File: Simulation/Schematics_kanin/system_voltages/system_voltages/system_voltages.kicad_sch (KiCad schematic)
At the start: 1 part

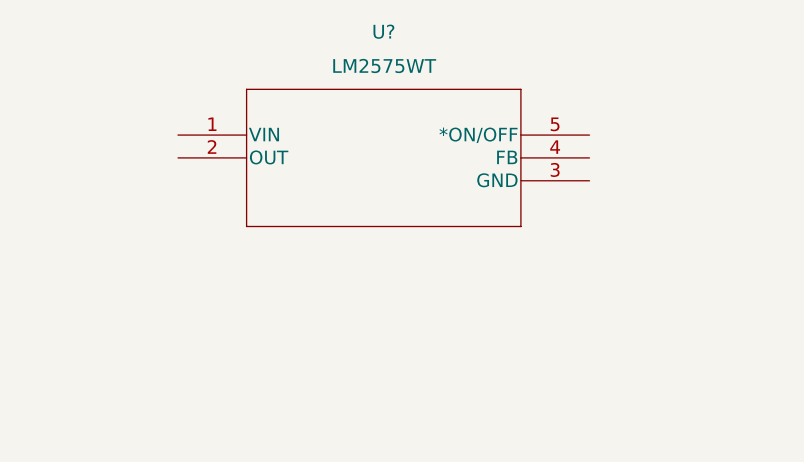
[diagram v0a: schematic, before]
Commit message: Made some changes for system voltages
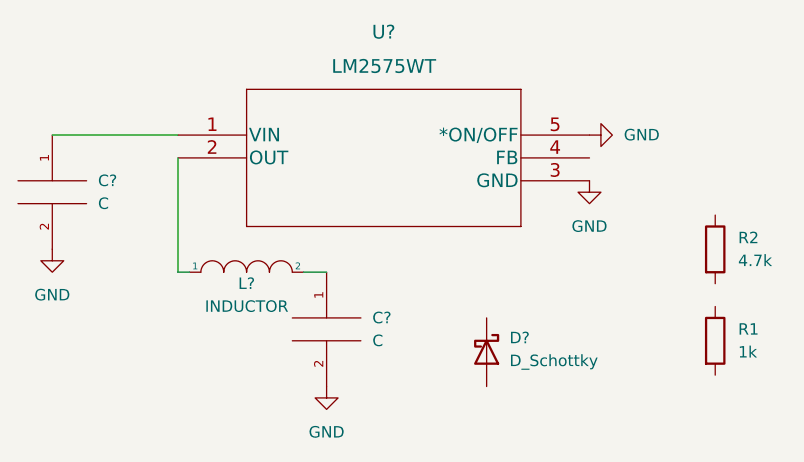
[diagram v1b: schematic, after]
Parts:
- added C? (x2): C, symbol pspice:C
- added D?: D_Schottky, symbol Device:D_Schottky
- added L?: INDUCTOR, symbol pspice:INDUCTOR
- added R1: 1k, symbol Device:R
- added R2: 4.7k, symbol Device:R
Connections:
- net at U?.1 (VIN): now also C?.1
- net at U?.2 (OUT): now also L?.1
- net GND: now reaches U?.3 (GND)
- net GND: now also U?.5 (*ON/OFF), C?.2, C?.2
- new net: C?.1, L?.2
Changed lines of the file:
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@@
 (kicad_sch (version 20211123) (generator eeschema)
   (paper "A4")
+  (wire (pts (xy 132.08 118.11) (xy 134.62 118.11))
+    (stroke (width 0) (type default) (color 0 0 0 0))
+  )
+  (wire (pts (xy 104.14 102.87) (xy 118.11 102.87))
+    (stroke (width 0) (type default) (color 0 0 0 0))
+  )
+  (wire (pts (xy 118.11 118.11) (xy 119.38 118.11))
+    (stroke (width 0) (type default) (color 0 0 0 0))
+  )
+  (wire (pts (xy 118.11 105.41) (xy 118.11 118.11))
+    (stroke (width 0) (type default) (color 0 0 0 0))
+  )
+  (symbol (lib_id "Device:D_Schottky") (at 152.4 127 270) (unit 1)
+    (in_bom yes) (on_board yes) (fields_autoplaced)
+    (property "Reference" "D?" (id 0) (at 154.94 125.4124 90)
+      (effects (font (size 1.27 1.27)) (justify left))
+    )
+    (property "Value" "D_Schottky" (id 1) (at 154.94 127.9524 90)
+      (effects (font (size 1.27 1.27)) (justify left))
+    )
+    (property "Footprint" "" (id 2) (at 152.4 127 0)
+      (effects (font (size 1.27 1.27)) hide)
+    )
+    (property "Datasheet" "~" (id 3) (at 152.4 127 0)
+      (effects (font (size 1.27 1.27)) hide)
+    )
+    (pin "1")
+    (pin "2")
+  )
   (symbol (lib_id "LM2575WT:LM2575WT") (at 118.11 102.87 0) (unit 1)
     (in_bom yes) (on_board yes) (fields_autoplaced)
@@
     (pin "5")
   )
+  (symbol (lib_id "power:GND") (at 163.83 107.95 0) (unit 1)
+    (in_bom yes) (on_board yes) (fields_autoplaced)
+    (property "Reference" "#PWR?" (id 0) (at 163.83 114.3 0)
+      (effects (font (size 1.27 1.27)) hide)
+    )
+    (property "Value" "GND" (id 1) (at 163.83 113.03 0))
+    (property "Footprint" "" (id 2) (at 163.83 107.95 0)
+      (effects (font (size 1.27 1.27)) hide)
+    )
+    (property "Datasheet" "" (id 3) (at 163.83 107.95 0)
+      (effects (font (size 1.27 1.27)) hide)
+    )
+    (pin "1")
+  )
+  (symbol (lib_id "Device:R") (at 177.8 115.57 0) (unit 1)
+    (in_bom yes) (on_board yes) (fields_autoplaced)
+    (property "Reference" "R2" (id 0) (at 180.34 114.2999 0)
+      (effects (font (size 1.27 1.27)) (justify left))
+    )
+    (property "Value" "4.7k" (id 1) (at 180.34 116.8399 0)
+      (effects (font (size 1.27 1.27)) (justify left))
+    )
+    (property "Footprint" "" (id 2) (at 176.022 115.57 90)
+      (effects (font (size 1.27 1.27)) hide)
+    )
+    (property "Datasheet" "~" (id 3) (at 177.8 115.57 0)
+      (effects (font (size 1.27 1.27)) hide)
+    )
+    (pin "1")
+    (pin "2")
+  )
+  (symbol (lib_id "power:GND") (at 163.83 102.87 90) (unit 1)
+    (in_bom yes) (on_board yes) (fields_autoplaced)
+    (property "Reference" "#PWR?" (id 0) (at 170.18 102.87 0)
+      (effects (font (size 1.27 1.27)) hide)
+    )
+    (property "Value" "GND" (id 1) (at 167.64 102.8699 90)
+      (effects (font (size 1.27 1.27)) (justify right))
+    )
+    (property "Footprint" "" (id 2) (at 163.83 102.87 0)
+      (effects (font (size 1.27 1.27)) hide)
+    )
+    (property "Datasheet" "" (id 3) (at 163.83 102.87 0)
+      (effects (font (size 1.27 1.27)) hide)
+    )
+    (pin "1")
+  )
+  (symbol (lib_id "pspice:C") (at 134.62 124.46 0) (unit 1)
+    (in_bom yes) (on_board yes) (fields_autoplaced)
+    (property "Reference" "C?" (id 0) (at 139.7 123.1899 0)
+      (effects (font (size 1.27 1.27)) (justify left))
+    )
+    (property "Value" "C" (id 1) (at 139.7 125.7299 0)
+      (effects (font (size 1.27 1.27)) (justify left))
+    )
+    (property "Footprint" "" (id 2) (at 134.62 124.46 0)
+      (effects (font (size 1.27 1.27)) hide)
+    )
+    (property "Datasheet" "~" (id 3) (at 134.62 124.46 0)
+      (effects (font (size 1.27 1.27)) hide)
+    )
+    (pin "1")
+    (pin "2")
+  )
+  (symbol (lib_id "power:GND") (at 134.62 130.81 0) (unit 1)
+    (in_bom yes) (on_board yes) (fields_autoplaced)
+    (property "Reference" "#PWR?" (id 0) (at 134.62 137.16 0)
+      (effects (font (size 1.27 1.27)) hide)
+    )
+    (property "Value" "GND" (id 1) (at 134.62 135.89 0))
+    (property "Footprint" "" (id 2) (at 134.62 130.81 0)
+      (effects (font (size 1.27 1.27)) hide)
+    )
+    (property "Datasheet" "" (id 3) (at 134.62 130.81 0)
+      (effects (font (size 1.27 1.27)) hide)
+    )
+    (pin "1")
+  )
+  (symbol (lib_id "power:GND") (at 104.14 115.57 0) (unit 1)
+    (in_bom yes) (on_board yes) (fields_autoplaced)
+    (property "Reference" "#PWR?" (id 0) (at 104.14 121.92 0)
+      (effects (font (size 1.27 1.27)) hide)
+    )
+    (property "Value" "GND" (id 1) (at 104.14 120.65 0))
+    (property "Footprint" "" (id 2) (at 104.14 115.57 0)
+      (effects (font (size 1.27 1.27)) hide)
+    )
+    (property "Datasheet" "" (id 3) (at 104.14 115.57 0)
+      (effects (font (size 1.27 1.27)) hide)
+    )
+    (pin "1")
+  )
+  (symbol (lib_id "Device:R") (at 177.8 125.73 0) (unit 1)
+    (in_bom yes) (on_board yes) (fields_autoplaced)
+    (property "Reference" "R1" (id 0) (at 180.34 124.4599 0)
+      (effects (font (size 1.27 1.27)) (justify left))
+    )
+    (property "Value" "1k" (id 1) (at 180.34 126.9999 0)
+      (effects (font (size 1.27 1.27)) (justify left))
+    )
+    (property "Footprint" "" (id 2) (at 176.022 125.73 90)
+      (effects (font (size 1.27 1.27)) hide)
+    )
+    (property "Datasheet" "~" (id 3) (at 177.8 125.73 0)
+      (effects (font (size 1.27 1.27)) hide)
+    )
+    (pin "1")
+    (pin "2")
+  )
+  (symbol (lib_id "pspice:C") (at 104.14 109.22 0) (unit 1)
+    (in_bom yes) (on_board yes) (fields_autoplaced)
+    (property "Reference" "C?" (id 0) (at 109.22 107.9499 0)
+      (effects (font (size 1.27 1.27)) (justify left))
+    )
+    (property "Value" "C" (id 1) (at 109.22 110.4899 0)
+      (effects (font (size 1.27 1.27)) (justify left))
+    )
+    (property "Footprint" "" (id 2) (at 104.14 109.22 0)
+      (effects (font (size 1.27 1.27)) hide)
+    )
+    (property "Datasheet" "~" (id 3) (at 104.14 109.22 0)
+      (effects (font (size 1.27 1.27)) hide)
+    )
+    (pin "1")
+    (pin "2")
+  )
+  (symbol (lib_id "pspice:INDUCTOR") (at 125.73 118.11 0) (unit 1)
+    (in_bom yes) (on_board yes)
+    (property "Reference" "L?" (id 0) (at 125.73 119.38 0))
+    (property "Value" "INDUCTOR" (id 1) (at 125.73 121.92 0))
+    (property "Footprint" "" (id 2) (at 125.73 118.11 0)
+      (effects (font (size 1.27 1.27)) hide)
+    )
+    (property "Datasheet" "~" (id 3) (at 125.73 118.11 0)
+      (effects (font (size 1.27 1.27)) hide)
+    )
+    (pin "1")
+    (pin "2")
+  )
   (sheet_instances
     (path "/" (page "1"))
   )
   (symbol_instances
+    (path "/4ce8880a-b1ac-40a1-8749-58cf3c00e4c1"
+      (reference "#PWR?") (unit 1) (value "GND") (footprint "")
+    )
+    (path "/6990307b-108e-4bc4-ae61-fe16d001e67f"
+      (reference "#PWR?") (unit 1) (value "GND") (footprint "")
+    )
+    (path "/eada501d-3f89-4d74-8dab-088438020409"
+      (reference "#PWR?") (unit 1) (value "GND") (footprint "")
+    )
+    (path "/ed3d533e-e353-4f6b-9e24-d383df13ee9c"
+      (reference "#PWR?") (unit 1) (value "GND") (footprint "")
+    )
+    (path "/b667fb33-fbff-4282-b694-1897b0d48a62"
+      (reference "C?") (unit 1) (value "C") (footprint "")
+    )
+    (path "/f65963e4-9e5d-496c-bda6-d160719668fe"
+      (reference "C?") (unit 1) (value "C") (footprint "")
+    )
+    (path "/1c7c2089-3376-4308-8f73-ac4f965a7e88"
+      (reference "D?") (unit 1) (value "D_Schottky") (footprint "")
+    )
+    (path "/fc4535f6-27e1-4a4e-83ff-d3a6850f1a18"
+      (reference "L?") (unit 1) (value "INDUCTOR") (footprint "")
+    )
+    (path "/f4a7a233-c755-4d67-a82c-9a2480fea3b4"
+      (reference "R1") (unit 1) (value "1k") (footprint "")
+    )
+    (path "/5ef24bb4-2e5f-4e8d-bbc3-030fcaf69a54"
+      (reference "R2") (unit 1) (value "4.7k") (footprint "")
+    )
     (path "/209a1b3a-c2b8-44bb-8fd3-4eec7e33a889"
       (reference "U?") (unit 1) (value "LM2575WT") (footprint "TO-220-5_MCH")

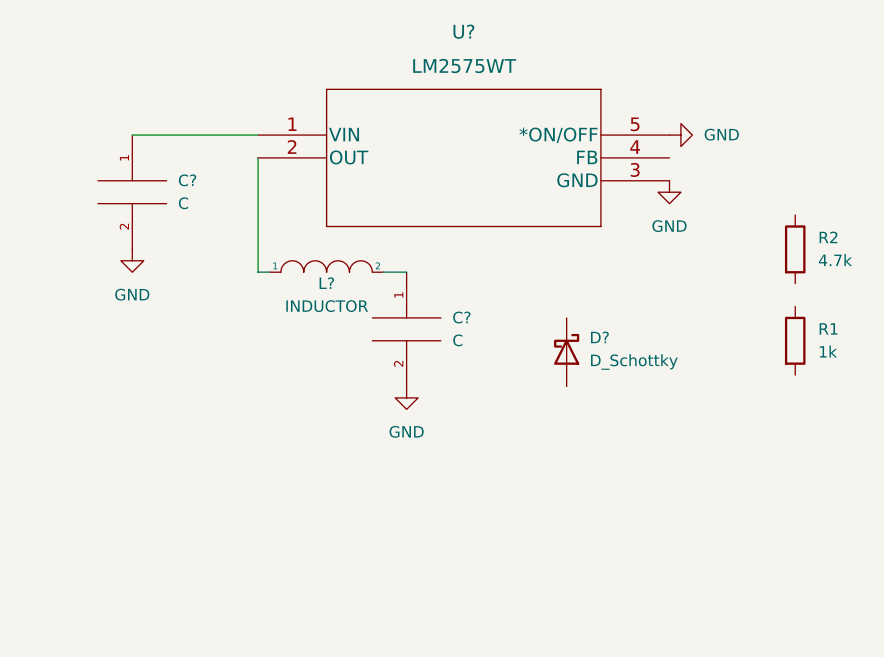
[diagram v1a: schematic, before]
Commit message: Added entry to Kanin's log + finished schematic of MCU 7V
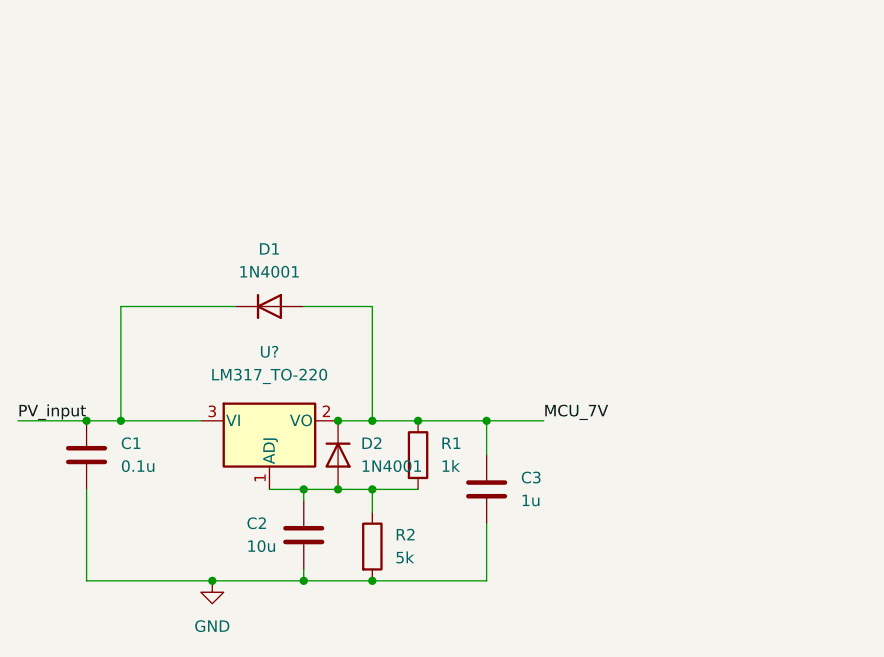
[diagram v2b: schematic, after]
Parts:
- removed C? (x2): C, symbol pspice:C
- removed D?: D_Schottky, symbol Device:D_Schottky
- removed L?: INDUCTOR, symbol pspice:INDUCTOR
- removed U?: LM2575WT, TO-220-5_MCH, symbol LM2575WT:LM2575WT
- added C1: 0.1u, symbol Device:C
- added C2: 10u, symbol Device:C
- added C3: 1u, symbol Device:C
- added D1, D2: 1N4001, Diode_THT:D_DO-41_SOD81_P10.16mm_Horizontal, symbol Diode:1N4001
- added U?: LM317_TO-220, Package_TO_SOT_THT:TO-220-3_Vertical, symbol Regulator_Linear:LM317_TO-220
- R2: value 4.7k -> 5k
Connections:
- net GND: now also R2.2, C1.2, C2.2, C3.2
- net at R2.1: now also R1.2, C2.1, D2.2 (A), U?.1 (ADJ)
- net MCU_7V: now reaches R1.1
- net MCU_7V: now also C3.1, D1.2 (A), D2.1 (K), U?.2 (VO)
- new net PV_input: C1.1, D1.1 (K), U?.3 (VI)

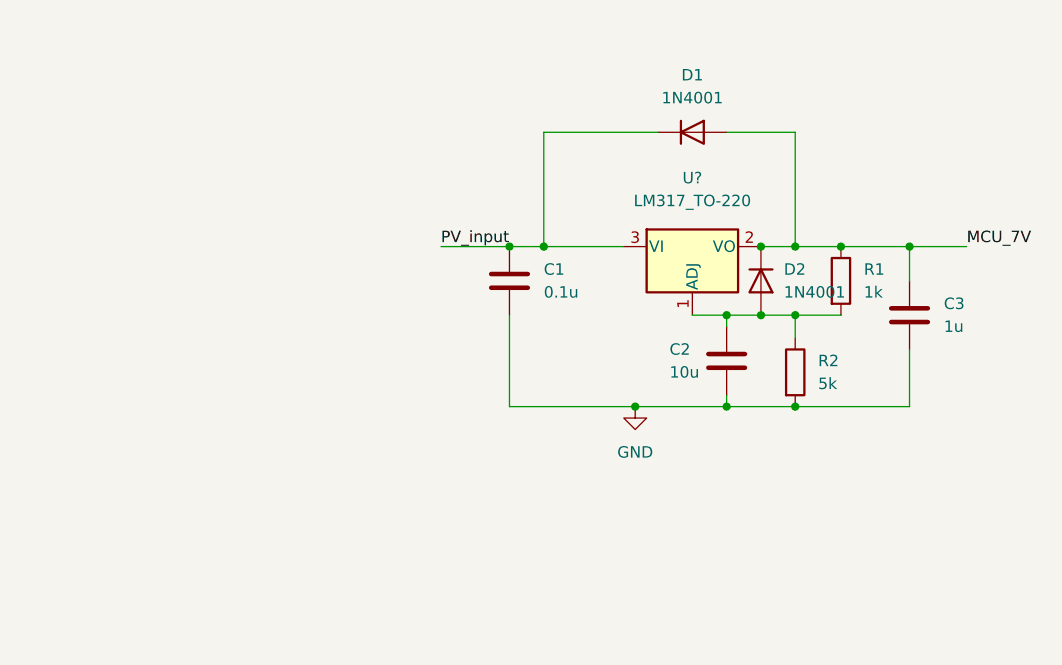
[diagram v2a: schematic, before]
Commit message: Updated 7 V MCU
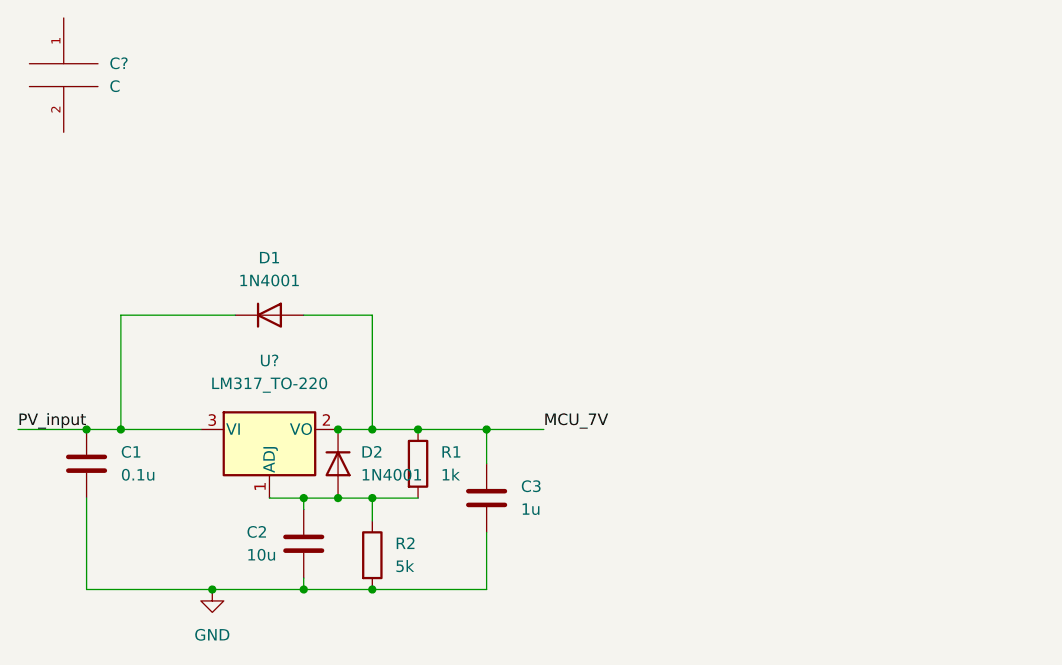
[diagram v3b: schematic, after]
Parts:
- added C?: C, symbol pspice:C
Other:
- moved on the sheet: C1, C2, C3, D1, D2, R1, R2, U?

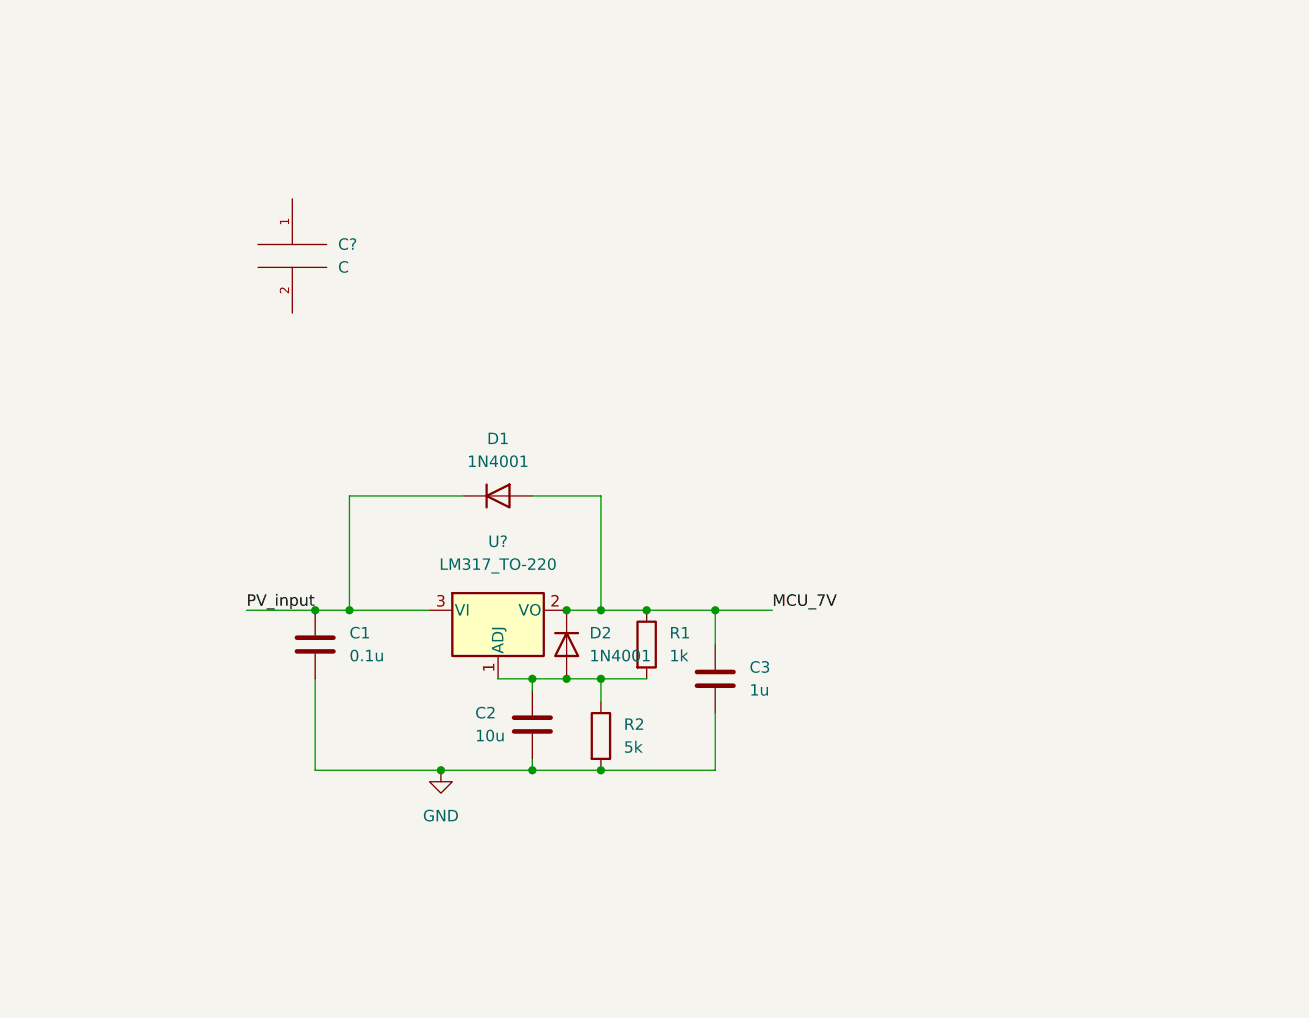
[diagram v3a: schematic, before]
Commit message: Added buck and USB charging
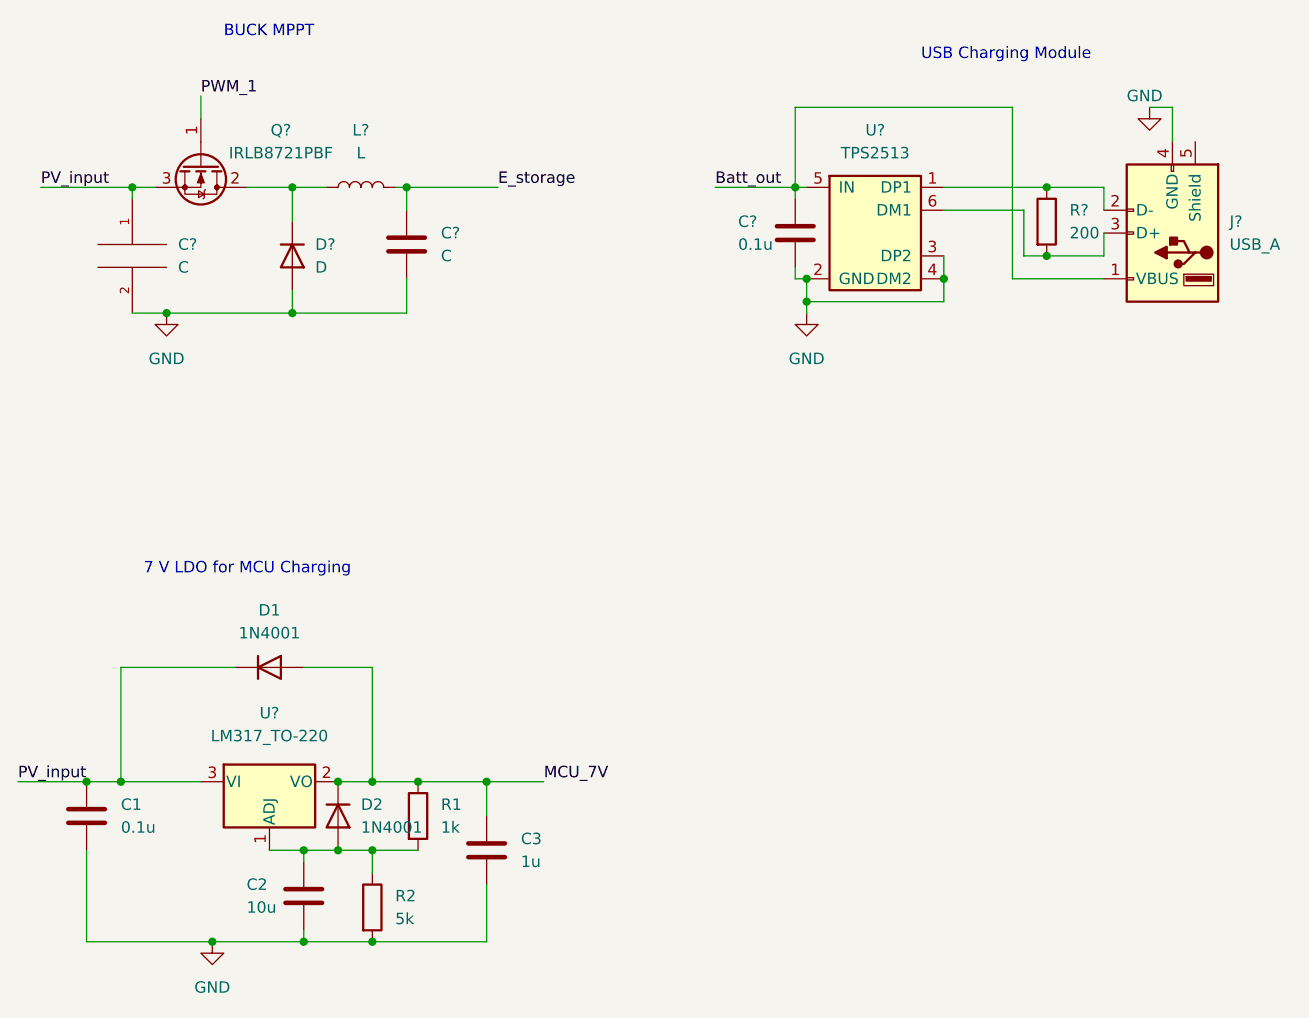
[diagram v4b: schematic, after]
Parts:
- added C?: C, symbol Device:C
- added C?: 0.1u, symbol Device:C
- added D?: D, symbol Device:D
- added J?: USB_A, symbol Connector:USB_A
- added L?: L, symbol Device:L
- added Q?: IRLB8721PBF, Package_TO_SOT_THT:TO-220-3_Vertical, symbol Transistor_FET:IRLB8721PBF
- added R?: 200, symbol Device:R
- added U?: TPS2513, Package_TO_SOT_SMD:SOT-23-6, symbol Interface_USB:TPS2513
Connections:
- net GND: now also C?.2, C?.2, C?.2, D?.2 (A), J?.4 (GND), U?.2 (GND), U?.3 (DP2), U?.4 (DM2)
- net PV_input: now also C?.1, Q?.3 (S)
- new net: J?.2 (D-), R?.1, U?.1 (DP1)
- new net: J?.3 (D+), R?.2, U?.6 (DM1)
- new net: D?.1 (K), L?.1, Q?.2 (D)
- new net Batt_out: C?.1, J?.1 (VBUS), U?.5 (IN)
- new net E_storage: C?.1, L?.2
- new net PWM_1: Q?.1 (G)
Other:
- note added: "7 V LDO for MCU Charging"
- note added: "BUCK MPPT"
- note added: "USB Charging Module"
- moved on the sheet: C1, C2, C3, C?, D1, D2, R1, R2, U?
